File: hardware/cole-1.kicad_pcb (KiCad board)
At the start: 4 copper layers, 100 x 100 mm, 37 parts, among them J1 PORT A, J2 PORT B, J3 TTL Serial, SW1 RESET, U1 WD65C02, U10 MC68B50, U11 74LS138, U2 ECS-2100AX-2.0MHZ, U3 MAX1232CPA, U4 AT28C256-15PU, U5 CY62256NLL-70PXC, U6 74HCT04, U7 74HCT32, U8 74HCT00, U9 WD65C22, Y1 1.8432 MHz

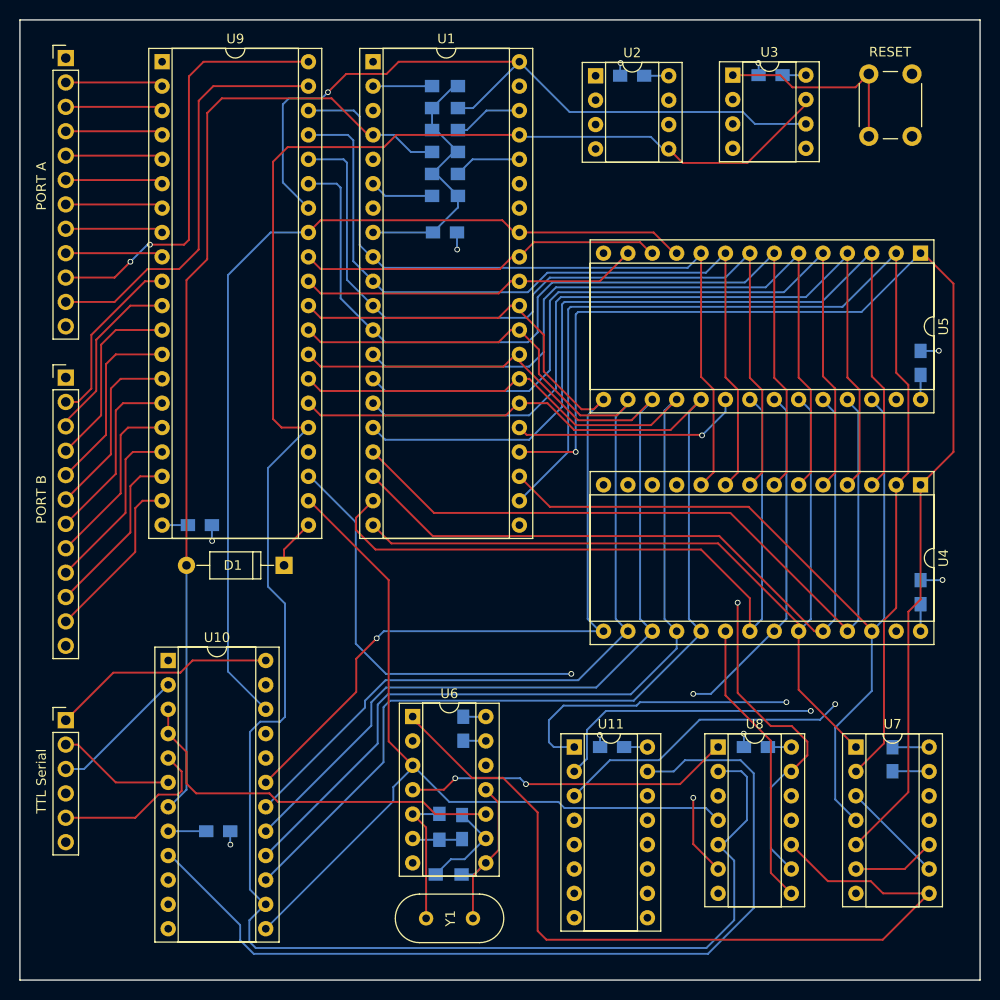
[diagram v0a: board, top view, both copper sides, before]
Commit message: Updated schematics, board layout, and GAL code for COLE-1+
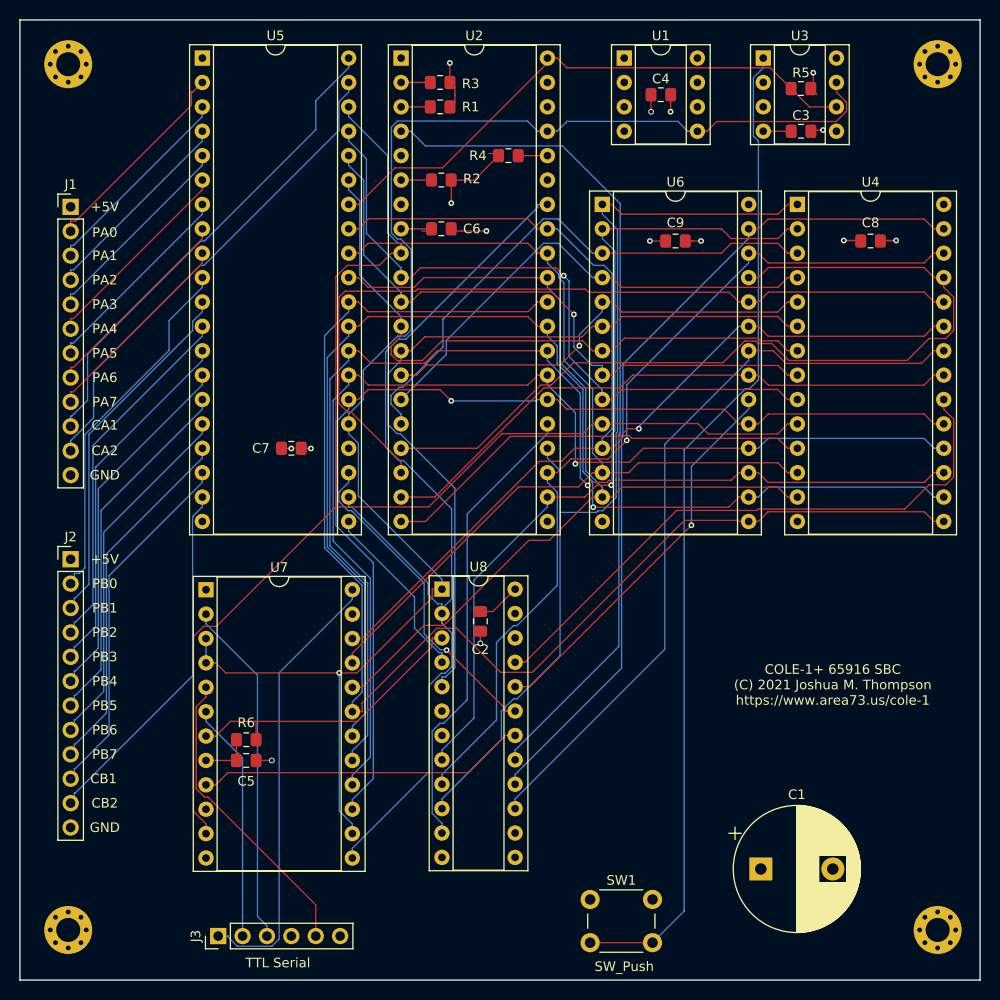
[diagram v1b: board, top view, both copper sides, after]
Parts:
- removed C10, C11: 0.1u, Capacitors_SMD:C_0805_HandSoldering
- removed C12: 270p, Capacitors_SMD:C_0805_HandSoldering
- removed D1: BA85, Diodes_THT:D_A-405_P10.16mm_Horizontal
- removed R7, R8: 2K2, Resistors_SMD:R_0805_HandSoldering
- removed R9: 3.3K, Resistors_SMD:R_0805_HandSoldering
- removed U10: MC68B50, Housings_DIP:DIP-24_W10.16mm_Socket
- removed U11: 74LS138, Housings_DIP:DIP-16_W7.62mm_Socket
- removed U9: WD65C22, Housings_DIP:DIP-40_W15.24mm_Socket
- removed Y1: 1.8432 MHz, Crystals:Crystal_HC49-U_Vertical
- added H1: MountingHole_Pad, MountingHole:MountingHole_2.5mm_Pad_Via, F.Cu at (97.4, 55.9)
- added H2: MountingHole_Pad, MountingHole:MountingHole_2.5mm_Pad_Via, F.Cu at (97.4, 146.1)
- added H3: MountingHole_Pad, MountingHole:MountingHole_2.5mm_Pad_Via, F.Cu at (188.0, 55.9)
- added H4: MountingHole_Pad, MountingHole:MountingHole_2.5mm_Pad_Via, F.Cu at (188.0, 146.1)
- added R5: 10k, Resistor_SMD:R_0805_2012Metric_Pad1.15x1.40mm_HandSolder, F.Cu at (173.7, 58.4)
- C1: value 0.1u -> 470uf; footprint Capacitors_SMD:C_0805_HandSoldering -> Capacitor_THT:CP_Radial_D13.0mm_P7.50mm; moved to F.Cu
- C2, C3, C4, C5, C6, C7, C8, C9: footprint Capacitors_SMD:C_0805_HandSoldering -> Capacitor_SMD:C_0805_2012Metric_Pad1.15x1.40mm_HandSolder; moved to F.Cu
- J1, J2: footprint Pin_Headers:Pin_Header_Straight_1x12_Pitch2.54mm -> Connector_PinHeader_2.54mm:PinHeader_1x12_P2.54mm_Vertical
- J3: footprint Pin_Headers:Pin_Header_Straight_1x06_Pitch2.54mm -> Connector_PinHeader_2.54mm:PinHeader_1x06_P2.54mm_Vertical
- R1, R2, R3, R4: footprint Resistors_SMD:R_0805_HandSoldering -> Resistor_SMD:R_0805_2012Metric_Pad1.15x1.40mm_HandSolder; moved to F.Cu
- R6: value 10k -> 3.3K; footprint Resistors_SMD:R_0805_HandSoldering -> Resistor_SMD:R_0805_2012Metric_Pad1.15x1.40mm_HandSolder; moved to F.Cu
- SW1: value RESET -> SW_Push; footprint Buttons_Switches_THT:SW_PUSH_6mm -> Button_Switch_THT:SW_PUSH_6mm_H5mm
- U1: value WD65C02 -> EC11TS-3.6864M; footprint Housings_DIP:DIP-40_W15.24mm_Socket -> Package_DIP:DIP-8_W7.62mm_Socket
- U2: value ECS-2100AX-2.0MHZ -> W65C816; footprint Housings_DIP:DIP-8_W7.62mm_Socket -> Package_DIP:DIP-40_W15.24mm_Socket
- U3: footprint Housings_DIP:DIP-8_W7.62mm_Socket -> Package_DIP:DIP-8_W7.62mm_Socket
- U4: footprint Housings_DIP:DIP-28_W15.24mm_Socket -> Package_DIP:DIP-28_W15.24mm_Socket
- U5: value CY62256NLL-70PXC -> WD65C22; footprint Housings_DIP:DIP-28_W15.24mm_Socket -> Package_DIP:DIP-40_W15.24mm_Socket
- U6: value 74HCT04 -> CY62256NLL-70PXC; footprint Housings_DIP:DIP-14_W7.62mm_Socket -> Package_DIP:DIP-28_W15.24mm_Socket
- U7: value 74HCT32 -> MC68B50; footprint Housings_DIP:DIP-14_W7.62mm_Socket -> Package_DIP:DIP-24_W15.24mm_Socket
- U8: value 74HCT00 -> CGL; footprint Housings_DIP:DIP-14_W7.62mm_Socket -> Package_DIP:DIP-24_W7.62mm_Socket
- moved SW1 92.3 mm to (151.8, 142.9), turned to 0 degrees
- moved C5 81.5 mm to (116.0, 128.4), turned to 180 degrees
- moved U5 77.5 mm to (111.4, 55.2), turned to 0 degrees
- moved C1 74.0 mm to (169.5, 139.7), turned to 0 degrees
- moved C7 70.5 mm to (120.7, 95.9), turned to 0 degrees
- moved U7 69.6 mm to (111.8, 110.6)
- moved R6 69.0 mm to (116.0, 126.2)
- moved C2 59.0 mm to (140.3, 113.9), turned to 90 degrees
- moved C4 58.5 mm to (159.1, 59.1), turned to 0 degrees
- moved C9 57.7 mm to (160.7, 74.3), turned to 0 degrees
- moved U6 56.9 mm to (153.0, 70.5)
- moved C8 54.0 mm to (181.0, 74.3)
- moved C6 52.1 mm to (136.3, 73.0), turned to 180 degrees
- moved U8 33.1 mm to (136.3, 110.6)
- moved U4 31.9 mm to (173.4, 70.5), turned to 0 degrees
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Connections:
- C1 pad 1: GND -> VCC
- C1 pad 2: VCC -> GND
- J1 pad 10: Net-(J1-Pad10) -> CA1
- J1 pad 11: Net-(J1-Pad11) -> CA2
- J1 pad 2: Net-(J1-Pad2) -> PA0
- J1 pad 3: Net-(J1-Pad3) -> PA1
- J1 pad 4: Net-(J1-Pad4) -> PA2
- J1 pad 5: Net-(J1-Pad5) -> PA3
- J1 pad 6: Net-(J1-Pad6) -> PA4
- J1 pad 7: Net-(J1-Pad7) -> PA5
- J1 pad 8: Net-(J1-Pad8) -> PA6
- J1 pad 9: Net-(J1-Pad9) -> PA7
- J2 pad 10: Net-(J2-Pad10) -> CB1
- J2 pad 11: Net-(J2-Pad11) -> CB2
- J2 pad 2: Net-(J2-Pad2) -> PB0
- J2 pad 3: Net-(J2-Pad3) -> PB1
- J2 pad 4: Net-(J2-Pad4) -> PB2
- J2 pad 5: Net-(J2-Pad5) -> PB3
- J2 pad 6: Net-(J2-Pad6) -> PB4
- J2 pad 7: Net-(J2-Pad7) -> PB5
- J2 pad 8: Net-(J2-Pad8) -> PB6
- J2 pad 9: Net-(J2-Pad9) -> PB7
- J3 pad 1: Net-(J3-Pad1) -> CTS
- J3 pad 2: Net-(J3-Pad2) -> TXD
- J3 pad 3: Net-(J3-Pad3) -> RXD
- J3 pad 5: Net-(J3-Pad5) -> RTS
- R6 pad 1: /Core Logic/RESET -> ~UARTIRQ
- U1 pad 1: Net-(U1-Pad1) -> (no net)
- U1 pad 2: Net-(R1-Pad1) -> (no net)
- U1 pad 3: Net-(U1-Pad3) -> (no net)
- U1 pad 4: /Core Logic/IRQ -> GND
- U1 pad 5: Net-(U1-Pad5) -> PHI2
- U1 pad 6: Net-(R4-Pad1) -> (no net)
- U1 pad 7: Net-(U1-Pad7) -> (no net)
- U2 pad 2: (no net) -> Net-(R3-Pad1)
- U2 pad 3: (no net) -> Net-(R1-Pad1)
- U2 pad 4: GND -> ~IRQ
- U2 pad 5: /Address Decoding/PHI2 -> (no net)
- U2 pad 6: (no net) -> Net-(R2-Pad1)
- U3 pad 5: Net-(U3-Pad5) -> (no net)
- U3 pad 6: /Core Logic/RESET -> ~RESET
- U3 pad 7: /Address Decoding/PHI2 -> PHI2
- U4 pad 1: /Address Decoding/A14 -> A14
- U4 pad 10: /Core Logic/A0 -> A0
- U4 pad 11: /Core Logic/D0 -> D0
- U4 pad 12: /Core Logic/D1 -> D1
- U4 pad 13: /Core Logic/D2 -> D2
- U4 pad 15: /Core Logic/D3 -> D3
- U4 pad 16: /Core Logic/D4 -> D4
- U4 pad 17: /Core Logic/D5 -> D5
- U4 pad 18: /Core Logic/D6 -> D6
- U4 pad 19: /Core Logic/D7 -> D7
- U4 pad 2: /Address Decoding/A12 -> A12
- U4 pad 20: /Address Decoding/ROMSEL -> ~ROMSEL
- U4 pad 21: /Core Logic/A10 -> A10
- U4 pad 22: /Address Decoding/RD -> ~RD
- U4 pad 23: /Address Decoding/A11 -> A11
- U4 pad 24: /Core Logic/A9 -> A9
- U4 pad 25: /Core Logic/A8 -> A8
- U4 pad 26: /Address Decoding/A13 -> A13
- U4 pad 27: VCC -> ~WR
- U4 pad 3: /Core Logic/A7 -> A7
- U4 pad 4: /Address Decoding/A6 -> A6
- U4 pad 5: /Address Decoding/A5 -> A5
- U4 pad 6: /Address Decoding/A4 -> A4
- U4 pad 7: /Core Logic/A3 -> A3
- U4 pad 8: /Core Logic/A2 -> A2
- U4 pad 9: /Core Logic/A1 -> A1
- U5 pad 1: /Address Decoding/A14 -> GND
- U5 pad 10: /Core Logic/A0 -> PB0
- U5 pad 11: /Core Logic/D0 -> PB1
- U5 pad 12: /Core Logic/D1 -> PB2
- U5 pad 13: /Core Logic/D2 -> PB3
- U5 pad 14: GND -> PB4
- U5 pad 15: /Core Logic/D3 -> PB5
- U5 pad 16: /Core Logic/D4 -> PB6
- U5 pad 17: /Core Logic/D5 -> PB7
- U5 pad 18: /Core Logic/D6 -> CB1
- U5 pad 19: /Core Logic/D7 -> CB2
- U5 pad 2: /Address Decoding/A12 -> PA0
- U5 pad 20: /Address Decoding/A15 -> VCC
- U5 pad 21: /Core Logic/A10 -> ~VIAIRQ
- U5 pad 22: /Address Decoding/RD -> R~W
- U5 pad 23: /Address Decoding/A11 -> ~VIASEL
- U5 pad 24: /Core Logic/A9 -> VCC
- U5 pad 25: /Core Logic/A8 -> PHI2
- U5 pad 26: /Address Decoding/A13 -> D7
- U5 pad 27: /Address Decoding/WR -> D6
- U5 pad 28: VCC -> D5
- U5 pad 3: /Core Logic/A7 -> PA1
- U5 pad 4: /Address Decoding/A6 -> PA2
- U5 pad 5: /Address Decoding/A5 -> PA3
- U5 pad 6: /Address Decoding/A4 -> PA4
- U5 pad 7: /Core Logic/A3 -> PA5
- U5 pad 8: /Core Logic/A2 -> PA6
- U5 pad 9: /Core Logic/A1 -> PA7
- U6 pad 1: Net-(U6-Pad1) -> A14
- U6 pad 10: Net-(U10-Pad3) -> A0
- U6 pad 11: Net-(R8-Pad1) -> D0
- U6 pad 12: Net-(U6-Pad12) -> D1
- U6 pad 13: GND -> D2
- U6 pad 14: VCC -> GND
- U6 pad 2: Net-(U6-Pad2) -> A12
- U6 pad 3: /Address Decoding/RWB -> A7
- U6 pad 4: Net-(U6-Pad4) -> A6
- U6 pad 5: Net-(R7-Pad2) -> A5
- U6 pad 6: Net-(C12-Pad2) -> A4
- U6 pad 7: GND -> A3
- U6 pad 8: Net-(R8-Pad1) -> A2
- U6 pad 9: Net-(C12-Pad1) -> A1
- U7 pad 1: /Address Decoding/A11 -> GND
- U7 pad 10: Net-(U7-Pad10) -> VCC
- U7 pad 11: Net-(U7-Pad11) -> A0
- U7 pad 12: GND -> VCC
- U7 pad 13: GND -> R~W
- U7 pad 14: VCC -> PHI2
- U7 pad 2: /Address Decoding/A12 -> RXD
- U7 pad 3: Net-(U7-Pad3) -> PHI2
- U7 pad 4: /Address Decoding/A13 -> PHI2
- U7 pad 5: /Address Decoding/A14 -> RTS
- U7 pad 6: Net-(U7-Pad10) -> TXD
- U7 pad 7: GND -> ~UARTIRQ
- U7 pad 8: Net-(U6-Pad1) -> VCC
- U7 pad 9: Net-(U7-Pad3) -> ~UARTSEL
- U8 pad 1: Net-(U6-Pad4) -> PHI2
- U8 pad 10: Net-(U6-Pad1) -> A14
- U8 pad 11: Net-(U11-Pad4) -> A15
- U8 pad 12: Net-(U6-Pad2) -> GND
- U8 pad 13: /Address Decoding/A15 -> (no net)
- U8 pad 14: VCC -> (no net)
- U8 pad 2: /Address Decoding/PHI2 -> R~W
- U8 pad 3: /Address Decoding/WR -> ~UARTIRQ
- U8 pad 4: /Address Decoding/RWB -> ~VIAIRQ
- U8 pad 5: /Address Decoding/PHI2 -> A4
- U8 pad 6: /Address Decoding/RD -> (no net)
- U8 pad 7: GND -> (no net)
- U8 pad 8: /Address Decoding/ROMSEL -> A12
- U8 pad 9: /Address Decoding/A15 -> A13
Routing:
- net /Address Decoding/PHI2: track 224.4 -> 0.00 mm
- net /Core Logic/D0: track 181.2 -> 0.00 mm
- net /Core Logic/A0: track 162.3 -> 0.00 mm
- net PHI2: track 0.00 -> 158.6 mm, vias 0 -> 1
- net A0: track 0.00 -> 143.5 mm
- net D3: track 0.00 -> 142.4 mm
- net /Address Decoding/A6: track 142.1 -> 0.00 mm, vias 1 -> 0
- net /Address Decoding/A5: track 135.8 -> 0.00 mm, vias 1 -> 0
- net /Address Decoding/RWB: track 134.2 -> 0.00 mm
- net /Address Decoding/A4: track 132.1 -> 0.00 mm, vias 1 -> 0
- net /Core Logic/D7: track 129.2 -> 0.00 mm
- net /Core Logic/D1: track 127.4 -> 0.00 mm
- net /Address Decoding/A14: track 126.1 -> 0.00 mm, vias 1 -> 0
- net D4: track 0.00 -> 125.9 mm, vias 0 -> 1
- net /Core Logic/D2: track 125.9 -> 0.00 mm
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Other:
- net class Default: clearance 0.2 -> 0.14; trace_width 0.2 -> 0.14
- rule trace_clearance: 0.2 -> 0.14
- rule trace_min: 0.15 -> 0.127
- rule via_min_drill: 0.3 -> 0.2
- rule via_min_size: 0.6 -> 0.4
- board text added: "+5V"
- board text added: "CA1"
- board text added: "CA2"
- board text added: "CB1"
- board text added: "CB2"
- board text added: "COLE-1+ 65916 SBC (C) 2021 Joshua M. Thompson https://www.area73.us/cole-1"
- board text added: "GND"
- board text added: "PA0"
- board text added: "PA1"
- board text added: "PA2"
- board text added: "PA3"
- board text added: "PA4"
- board text added: "PA5"
- board text added: "PA6"
- board text added: "PA7"
- board text added: "PB0"
- board text added: "PB1"
- board text added: "PB2"
- board text added: "PB3"
- board text added: "PB4"
- board text added: "PB5"
- board text added: "PB6"
- board text added: "PB7"

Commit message: Add A10 and A11 routing to GAL, and update GAL equations
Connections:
- U8 pad 6: (no net) -> A10
- U8 pad 7: (no net) -> A11
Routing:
- net A8: track 91.4 -> 65.3 mm, vias 0 -> 1
- net A11: track 65.9 -> 91.1 mm
- net A0: track 143.5 -> 168.2 mm
- net A10: track 62.6 -> 87.1 mm, vias 0 -> 1
- net VCC: track 40.0 -> 17.0 mm, vias 8 -> 12
- net A9: track 85.9 -> 65.2 mm, vias 0 -> 1
- net A2: track 66.2 -> 83.9 mm, vias 1 -> 0
- net A6: track 51.2 -> 66.4 mm
- net A5: track 46.6 -> 60.3 mm, vias 1 -> 0
- net D2: track 102.2 -> 113.7 mm
- net D1: track 102.8 -> 113.5 mm
- net ~IRQ: track 88.4 -> 78.2 mm, vias 0 -> 1
- net D0: track 104.5 -> 113.6 mm
- net GND: track 17.2 -> 8.63 mm, vias 7 -> 8
- net A14: track 102.3 -> 95.9 mm
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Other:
- board text added: "COLE-1+ 65916 SBC (C) 2021 Joshua M. Thompson https://www.area73.us/cole-1-plus"
- board text removed: "COLE-1+ 65916 SBC (C) 2021 Joshua M. Thompson https://www.area73.us/cole-1"
